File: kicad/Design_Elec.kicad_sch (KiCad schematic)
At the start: 0 parts

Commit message: Shematic, Atmega and J1/2
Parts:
- added ATmega328P-A1: ~, symbol Symbol_lib:ATmega328P-A
- added C1: 100nF, symbol Symbol_lib:C_100nF
- added GND: ~, symbol Symbol_lib:GND
- added J1, J2: ~, symbol Symbol_lib:J_12Pin
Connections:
- new net: ATmega328P-A1.20 (AREF), C1.
- new net: ATmega328P-A1.3 (GND), GND.
- new net: ATmega328P-A1.18 (AVCC), ATmega328P-A1.4 (VCC)
- new net A0: ATmega328P-A1.23 (PC0), J2.8
- new net A1: ATmega328P-A1.24 (PC1), J2.7
- new net A2: ATmega328P-A1.25 (PC2), J2.6
- new net A3: ATmega328P-A1.26 (PC3), J2.5
- new net A4: ATmega328P-A1.27 (PC4)
- new net A5: ATmega328P-A1.28 (PC5)
- new net A6: ATmega328P-A1.19 (ADC6)
- new net A7: ATmega328P-A1.22 (ADC7)
- new net D10: ATmega328P-A1.14 (PB2), J2.12
- new net D2: ATmega328P-A1.32 (PD2), J1.8
- new net D3: ATmega328P-A1.1 (PD3), J1.7
- new net D4: ATmega328P-A1.2 (PD4), J1.6
- new net D5: ATmega328P-A1.9 (PD5), J1.5
- new net D6: ATmega328P-A1.10 (PD6), J1.4
- new net D7: ATmega328P-A1.11 (PD7), J1.3
- new net D8: ATmega328P-A1.12 (PB0), J1.2
- new net D9: ATmega328P-A1.13 (PB1), J1.1
- new net GND: J1.9, J2.2
- new net MISO: ATmega328P-A1.16 (PB4), J2.10
- new net MOSI: ATmega328P-A1.15 (PB3), J2.11
- new net RAW: J2.1
- new net RST: ATmega328P-A1.29 (RESET/PC6), J1.10, J2.3
- new net RXI: ATmega328P-A1.30 (PD0), J1.11
- new net SCK: ATmega328P-A1.17 (PB5), J2.9
- new net TXO: ATmega328P-A1.31 (PD1), J1.12
- new net VCC: J2.4

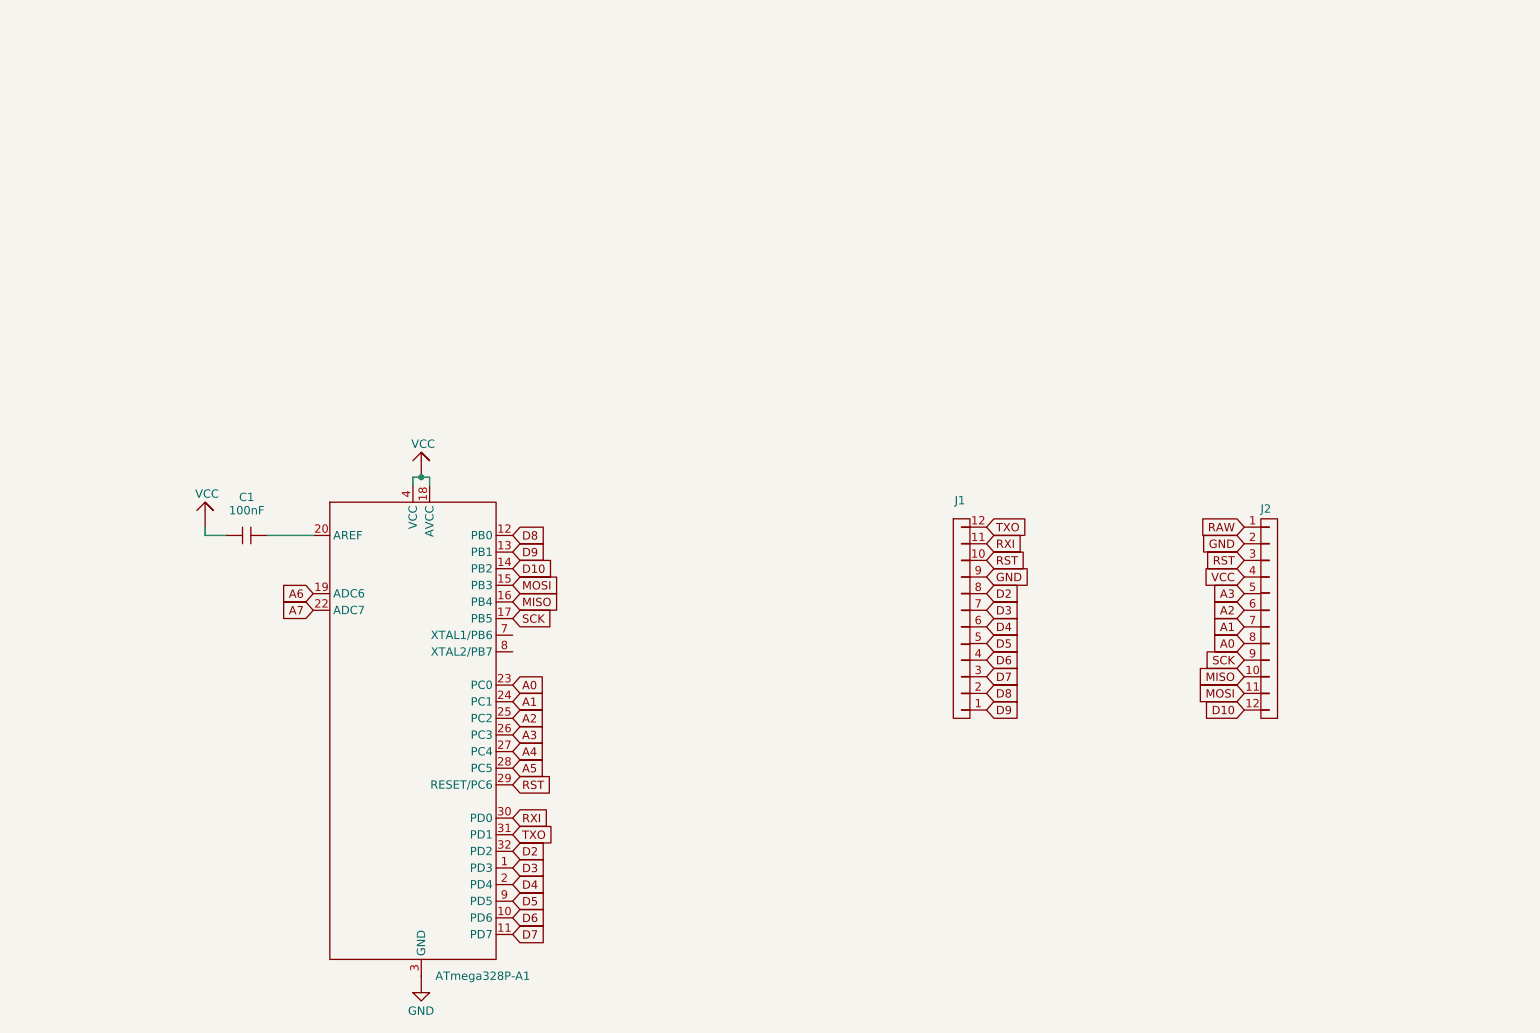
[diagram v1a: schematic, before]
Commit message: Shematic - Down is made
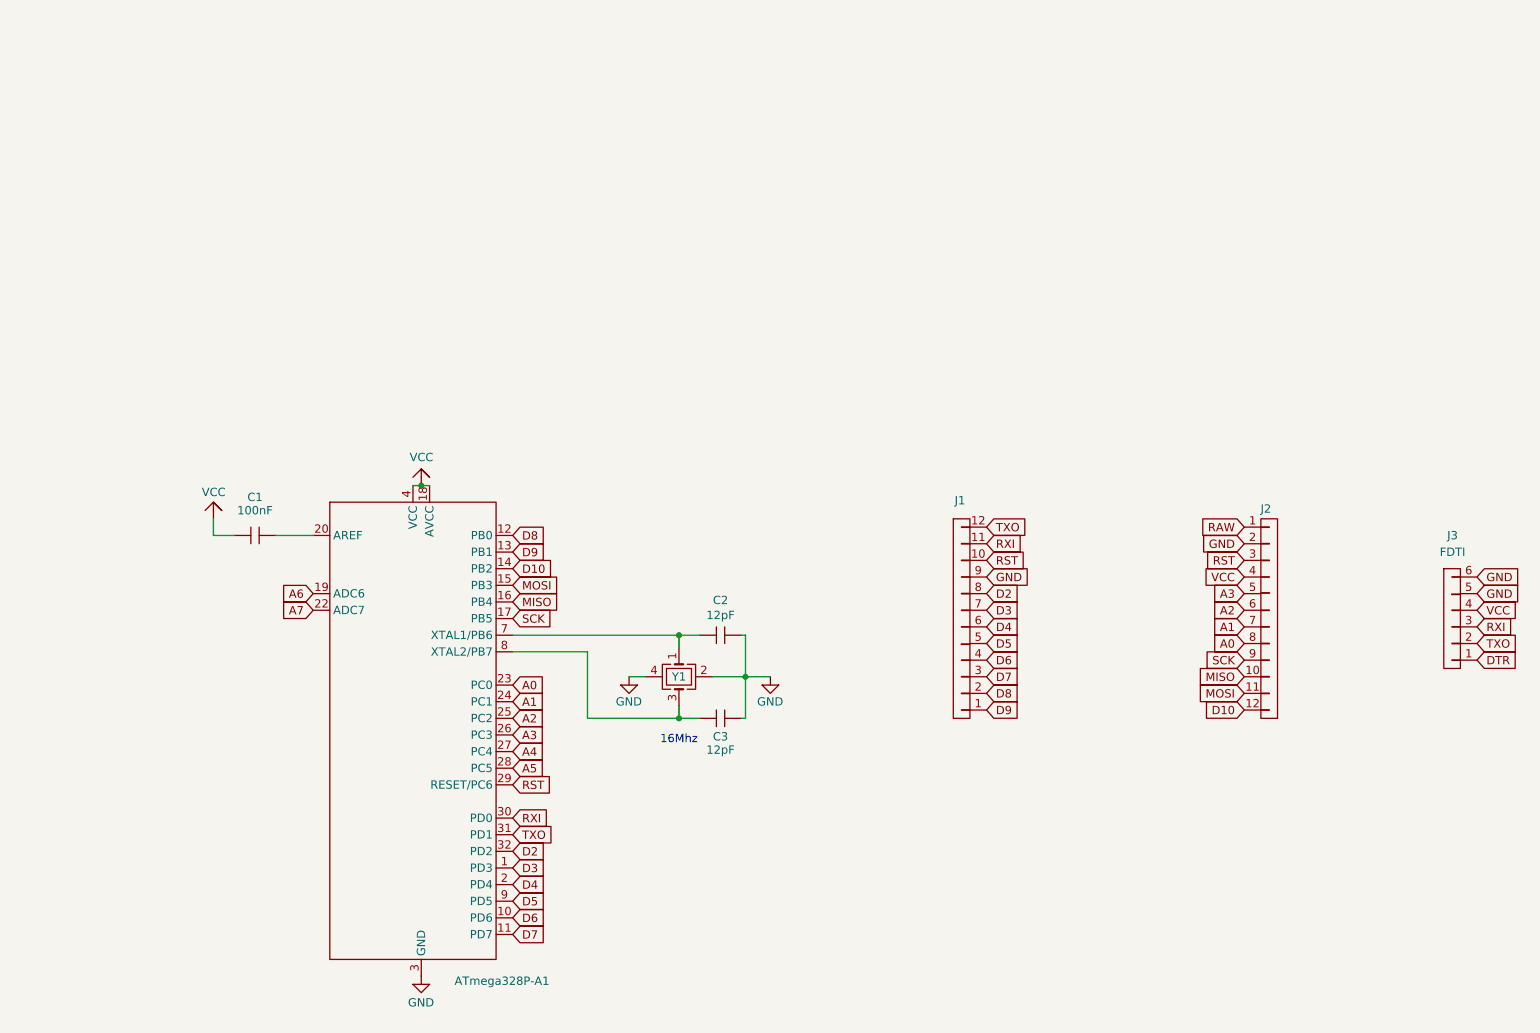
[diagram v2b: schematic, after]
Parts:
- added C2, C3: 12pF, symbol Symbol_lib:C_12pF
- added GND (x2): ~, symbol Symbol_lib:GND
- added J3: FDTI, symbol Symbol_lib:J_6Pin
- added Y1: ~, symbol Symbol_lib:Y
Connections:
- net GND: now also J3.5, J3.6
- net RXI: now also J3.3
- net TXO: now also J3.2
- net VCC: now also J3.4
- net at C1.: now also ATmega328P-A1.20 (AREF)
- net at ATmega328P-A1.7 (XTAL1/PB6): now also C2., Y1.1
- net at ATmega328P-A1.8 (XTAL2/PB7): now also C3., Y1.3
- new net: C2., C3., GND., Y1.2
- new net: GND., Y1.4
- new net DTR: J3.1
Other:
- note added: "16Mhz"
- moved on the sheet: C1, GND

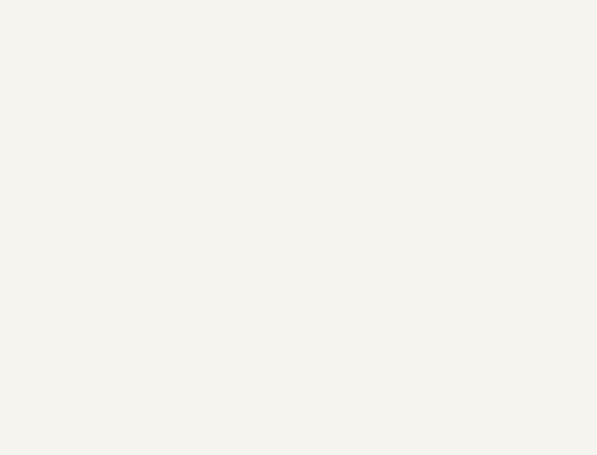
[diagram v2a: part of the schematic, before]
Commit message: Symbol table is 50mm aligned
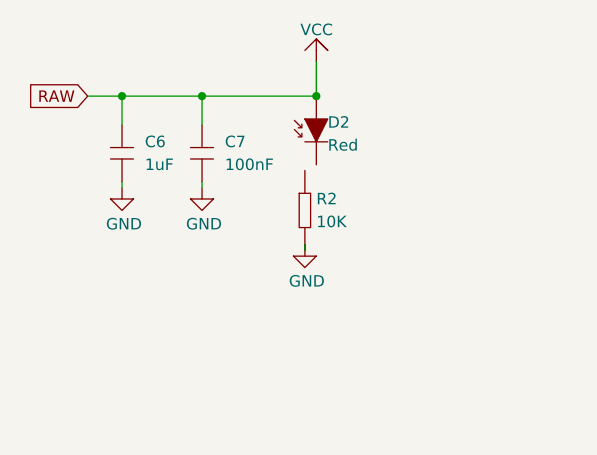
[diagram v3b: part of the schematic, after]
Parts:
- added C6: 1uF, symbol Symbol_lib:C_1uF
- added C7: 100nF, symbol Symbol_lib:C_100nF
- added D2: Red, symbol Symbol_lib:LED_Red
- added GND (x3): ~, symbol Symbol_lib:GND
- added R2: 10K, symbol Symbol_lib:R_10kΩ
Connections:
- net RAW: now also C6., C7., D2.
- net at C1.: now also ATmega328P-A1.20 (AREF)
- new net: C7., GND.
- new net: C6., GND.
- new net: GND., R2.

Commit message: Shematic done ?? idk
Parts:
- added C4: 100nF, symbol Symbol_lib:C_100nF
- added D1: Green, symbol Symbol_lib:LED_Green
- added GND (x2): ~, symbol Symbol_lib:GND
- added R1: 330, symbol Symbol_lib:R_330Ω
- added R3: 10K, symbol Symbol_lib:R_10kΩ
- added SW1: SW_Push, symbol Symbol_lib:Switch
- renumbered C3 to C1
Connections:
- net RST is gone; now on net DTR: ATmega328P-A1.29 (RESET/PC6), J1.10, J2.3
- net DTR: now also R3., SW1.
- net SCK: now also R1.
- net at C1.: now also ATmega328P-A1.20 (AREF)
- new net: C4., GND.
- new net: C4., SW1.
- new net: D1., R1.
- new net: D2., R2.
- new net: D1., GND.
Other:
- moved on the sheet: C1, C2, C6, C7, D2, GND, J1, J2, J3, R2, Y1

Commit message: No idea why it doesnt not work no idea why it should
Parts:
- removed ATmega328P-A1: ~, symbol Symbol_lib:ATmega328P-A
- removed C1, C4, C7: 100nF, symbol Symbol_lib:C_100nF
- removed C1, C2: 12pF, symbol Symbol_lib:C_12pF
- removed C6: 1uF, symbol Symbol_lib:C_1uF
- removed D1: Green, symbol Symbol_lib:LED_Green
- removed D2: Red, symbol Symbol_lib:LED_Red
- removed GND (x8): ~, symbol Symbol_lib:GND
- removed R1: 330, symbol Symbol_lib:R_330Ω
- removed R2, R3: 10K, symbol Symbol_lib:R_10kΩ
- added C1, C2: 12pF, symbol Symbol_lib:C
- added C3, C4, C7: 100nf, symbol Symbol_lib:C
- added C6: 1uF, symbol Symbol_lib:C
- added D1: Green, symbol Symbol_lib:LED
- added D2: Red, symbol Symbol_lib:LED
- added R1: 330, symbol Symbol_lib:R
- added R2, R3: 10K, symbol Symbol_lib:R
- added U1: ATmega328P-A, symbol Symbol_lib:ATmega328P-A
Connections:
- net RAW is gone; now on net VCC: J2.1
- net A0: now also U1.23 (PC0)
- net A1: now also U1.24 (PC1)
- net A2: now also U1.25 (PC2)
- net A3: now also U1.26 (PC3)
- net A4: now also U1.27 (PC4)
- net A5: now also U1.28 (PC5)
- net A6: now also U1.19 (ADC6)
- net A7: now also U1.22 (ADC7)
- net D10: now also U1.14 (PB2)
- net D2: now also U1.32 (PD2)
- net D3: now also U1.1 (PD3)
- net D4: now also U1.2 (PD4)
- net D5: now also U1.9 (PD5)
- net D6: now also U1.10 (PD6)
- net D7: now also U1.11 (PD7)
- net D8: now also U1.12 (PB0)
- net D9: now also U1.13 (PB1)
- net DTR: now also R3., U1.29 (RESET/PC6)
- net GND: now also Y1.2, Y1.4, C1., C2., C4., C6., C7., D1., R2., U1.3 (GND)
- net MISO: now also U1.16 (PB4)
- net MOSI: now also U1.15 (PB3)
- net RXI: now also U1.30 (PD0)
- net SCK: now also R1., U1.17 (PB5)
- net TXO: now also U1.31 (PD1)
- net VCC: now also C3., C6., C7., D2., R3., U1.18 (AVCC), U1.4 (VCC)
- net at Y1.1: now also C2., U1.7 (XTAL1/PB6)
- net at Y1.3: now also C1., U1.8 (XTAL2/PB7)
- new net: D1., R1.
- new net: C4., SW1.
- new net: C3., U1.20 (AREF)
- new net: D2., R2.

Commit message: Pins are numbers, only 2 errors
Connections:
- net DTR: now also R3.2, SW1.2; no longer R3., SW1.
- net GND: now also C1.2, C2.2, C4.1, C6.2, C7.2, D1.1, R2.2; no longer C1., C2., C4., C6., C7., D1., R2.
- net SCK: now also R1.1; no longer R1.
- net VCC: now also C3.1, C6.1, C7.1, D2.2, R3.1; no longer C3., C6., C7., D2., R3.
- net at U1.8 (XTAL2/PB7), Y1.3: now also C1.1; no longer C1.
- net at U1.20 (AREF): now also C3.2; no longer C3.
- net at U1.7 (XTAL1/PB6), Y1.1: now also C2.1; no longer C2.
- new net: D1.2, R1.2
- new net: C4.2, SW1.1
- new net: D2.1, R2.1
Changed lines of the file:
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@@
 	)
 	(symbol
-		(lib_name "R_1")
 		(lib_id "Symbol_lib:R")
 		(at 110.49 39.37 0)
@@
 			)
 		)
-		(pin ""
-		)
-		(pin ""
+		(pin "1"
+		)
+		(pin "2"
 		)
 		(instances
@@
 	)
 	(symbol
-		(lib_name "C_3")
 		(lib_id "Symbol_lib:C")
 		(at 152.4 41.91 90)
@@
 			)
 		)
-		(pin ""
-		)
-		(pin ""
+		(pin "1"
+		)
+		(pin "2"
 		)
 		(instances
@@
 	)
 	(symbol
-		(lib_name "C_5")
 		(lib_id "Symbol_lib:C")
 		(at 127 123.19 90)
@@
 			)
 		)
-		(pin ""
-		)
-		(pin ""
+		(pin "2"
+		)
+		(pin "1"
 		)
 		(instances
@@
 			)
 		)
-		(pin ""
-		)
-		(pin ""
+		(pin "2"
+		)
+		(pin "1"
 		)
 		(instances
@@
 	)
 	(symbol
-		(lib_name "C_2")
 		(lib_id "Symbol_lib:C")
 		(at 54.61 45.72 0)
@@
 			)
 		)
-		(pin ""
-		)
-		(pin ""
+		(pin "2"
+		)
+		(pin "1"
 		)
 		(instances
@@
 	)
 	(symbol
-		(lib_name "C_1")
 		(lib_id "Symbol_lib:C")
 		(at 127 111.76 90)
@@
 			)
 		)
-		(pin ""
-		)
-		(pin ""
+		(pin "1"
+		)
+		(pin "2"
 		)
 		(instances
@@
 			)
 		)
-		(pin ""
-		)
-		(pin ""
+		(pin "2"
+		)
+		(pin "1"
 		)
 		(instances
@@
 	)
 	(symbol
-		(lib_name "C_4")
 		(lib_id "Symbol_lib:C")
 		(at 45.72 45.72 0)
@@
 			)
 		)
-		(pin ""
-		)
-		(pin ""
+		(pin "2"
+		)
+		(pin "1"
 		)
 		(instances
@@
 	)
 	(symbol
-		(lib_name "LED_1")
 		(lib_id "Symbol_lib:LED")
 		(at 67.31 43.18 0)
@@
 			)
 		)
-		(pin ""
-		)
-		(pin ""
+		(pin "2"
+		)
+		(pin "1"
 		)
 		(instances
@@
 			)
 		)
-		(pin ""
-		)
-		(pin ""
+		(pin "2"
+		)
+		(pin "1"
 		)
 		(instances
@@
 			)
 		)
-		(pin ""
-		)
-		(pin ""
+		(pin "2"
+		)
+		(pin "1"
 		)
 		(instances
@@
 	)
 	(symbol
-		(lib_name "R_2")
 		(lib_id "Symbol_lib:R")
 		(at 166.37 38.1 0)
@@
 			)
 		)
-		(pin ""
-		)
-		(pin ""
-		)
-		(instances
+		(pin "2"
+		)
+		(pin "1"
+		)
+		(instances
